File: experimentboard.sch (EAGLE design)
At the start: 173 parts, among them IC1 TL072P, IC2 LM317, IC3 LM337, IC4 TL072P, IC5 TL072P, IC6 TL072P, P1 PLR135/T9, P9 P9, U1 PCM1690, U2 DIR9001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

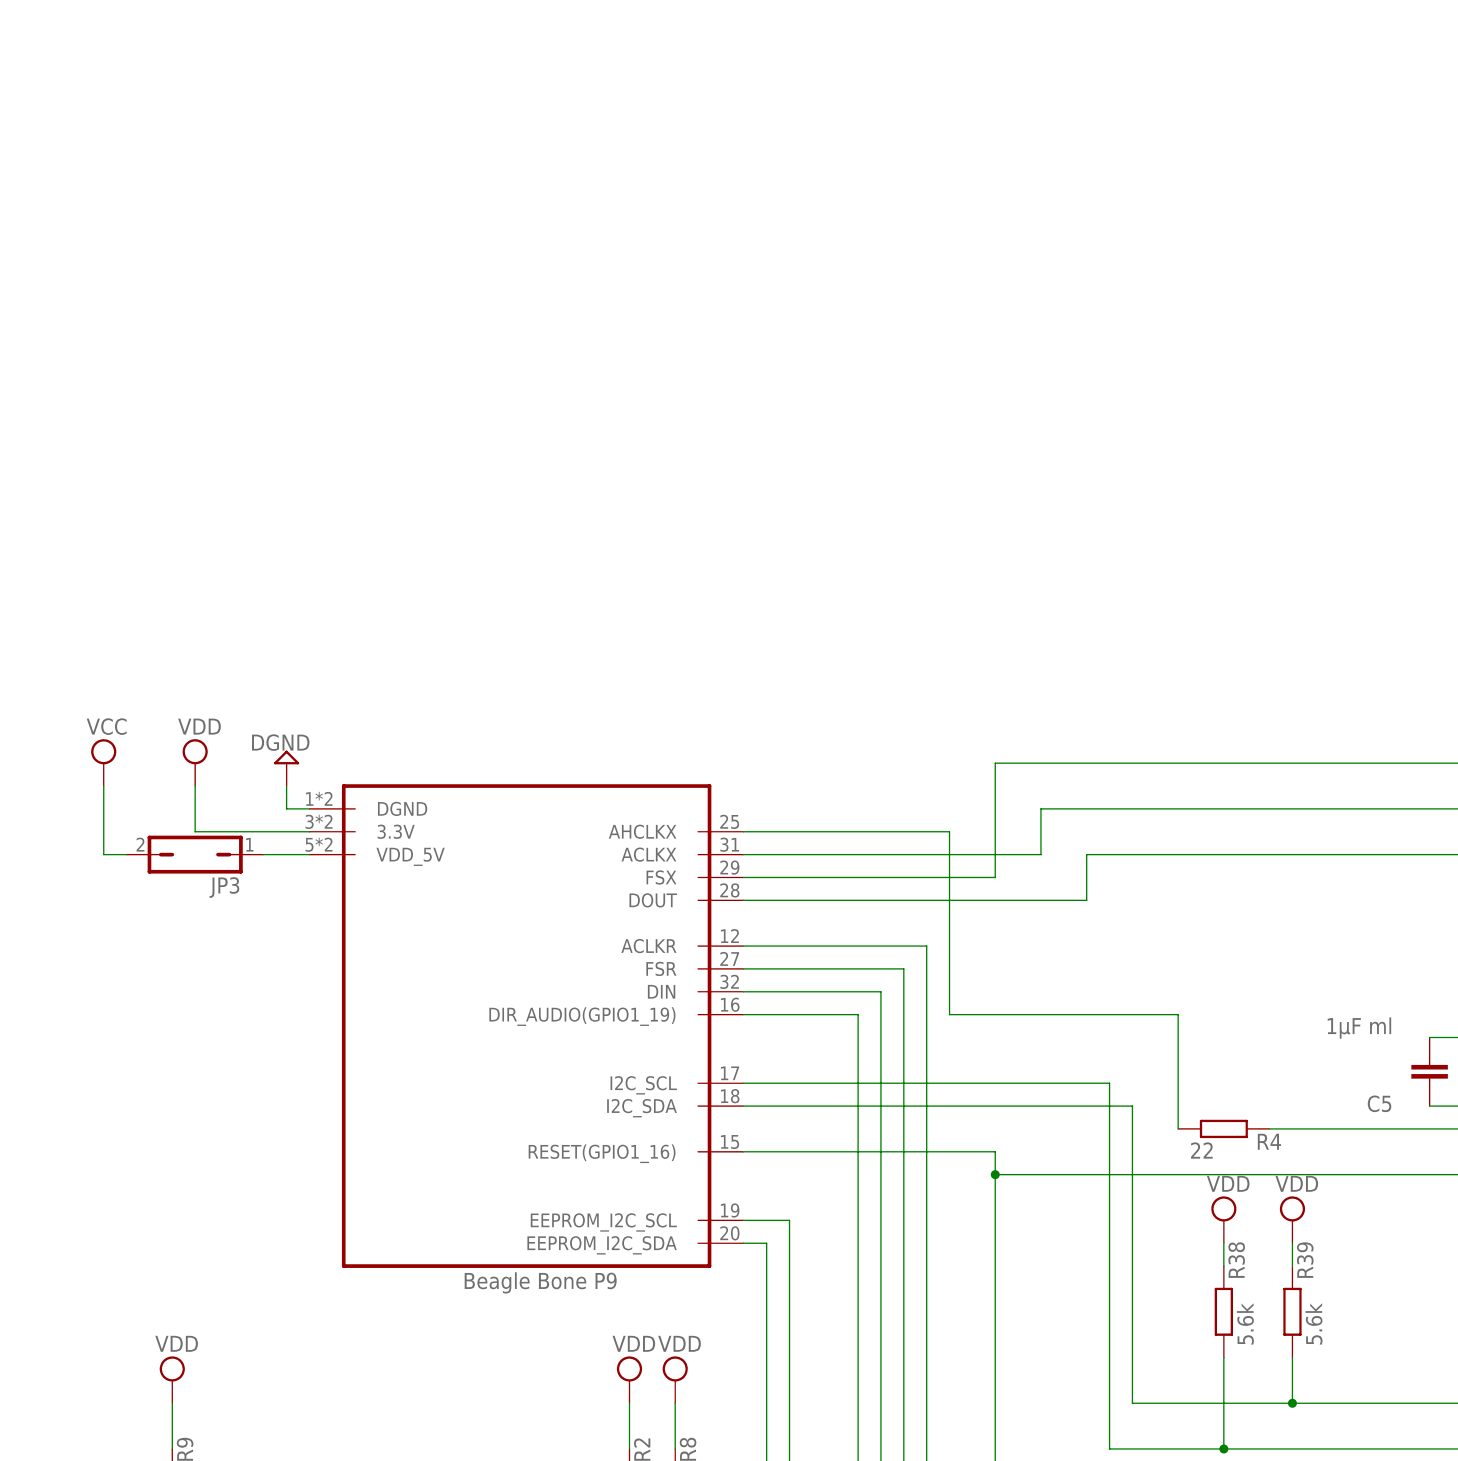
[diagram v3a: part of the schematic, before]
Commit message: Added two status LEDs
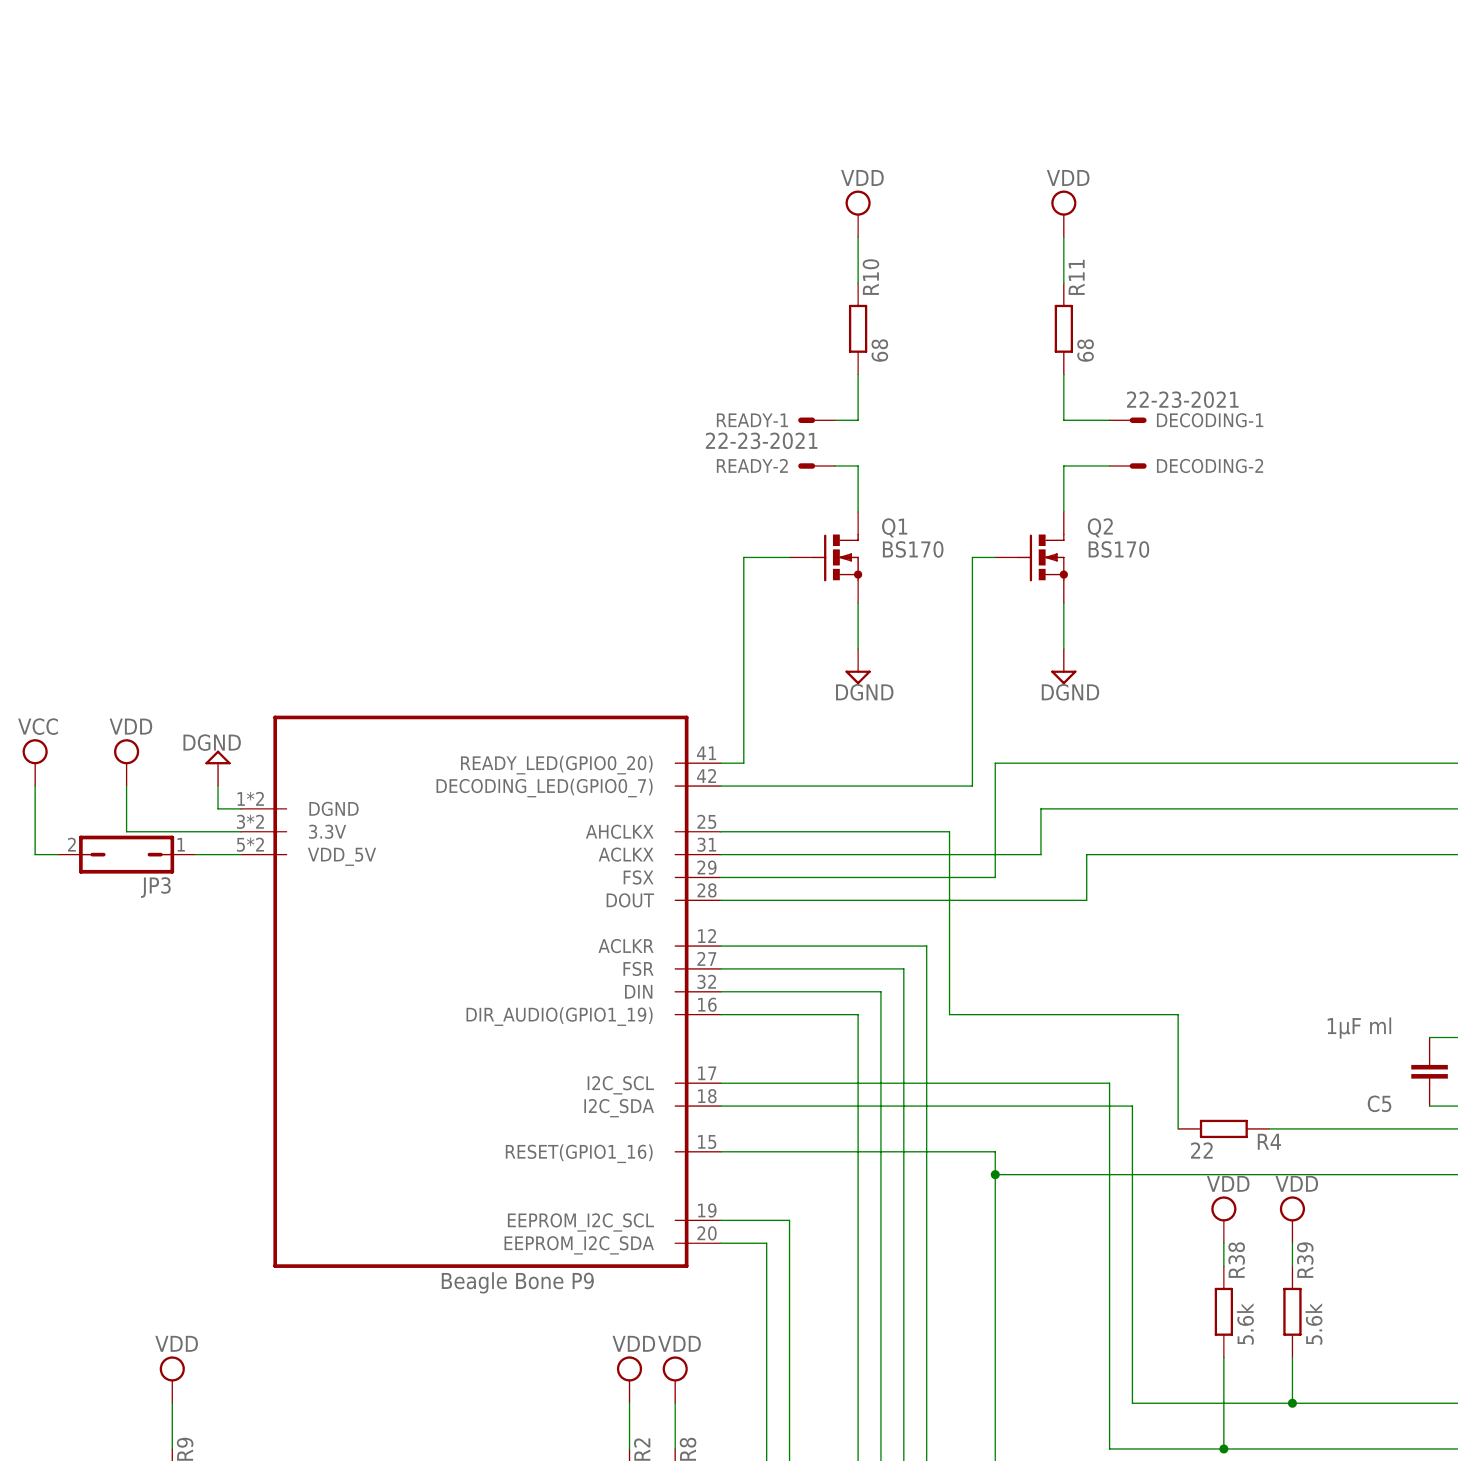
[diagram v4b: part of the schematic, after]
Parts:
- added DECODING, READY: 22-23-2021, con-molex:22-23-2021
- added Q1, Q2: BS170, transistor-small-signal:BS170
- added R10, R11: 68, rcl:R-EU_0204/2V
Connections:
- new net N$28: R10.1, READY-1.S
- new net N$4: Q1.D, READY-2.S
- new net N$91: DECODING-2.S, Q2.D
- new net N$92: DECODING-1.S, R11.1
- new net N$93: P9.READY_LED(GPIO0_20), Q1.G
- new net N$94: P9.DECODING_LED(GPIO0_7), Q2.G
- net DGND: now also Q1.S, Q2.S
- net VDD: now also R10.2, R11.2
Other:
- moved on the sheet: JP3

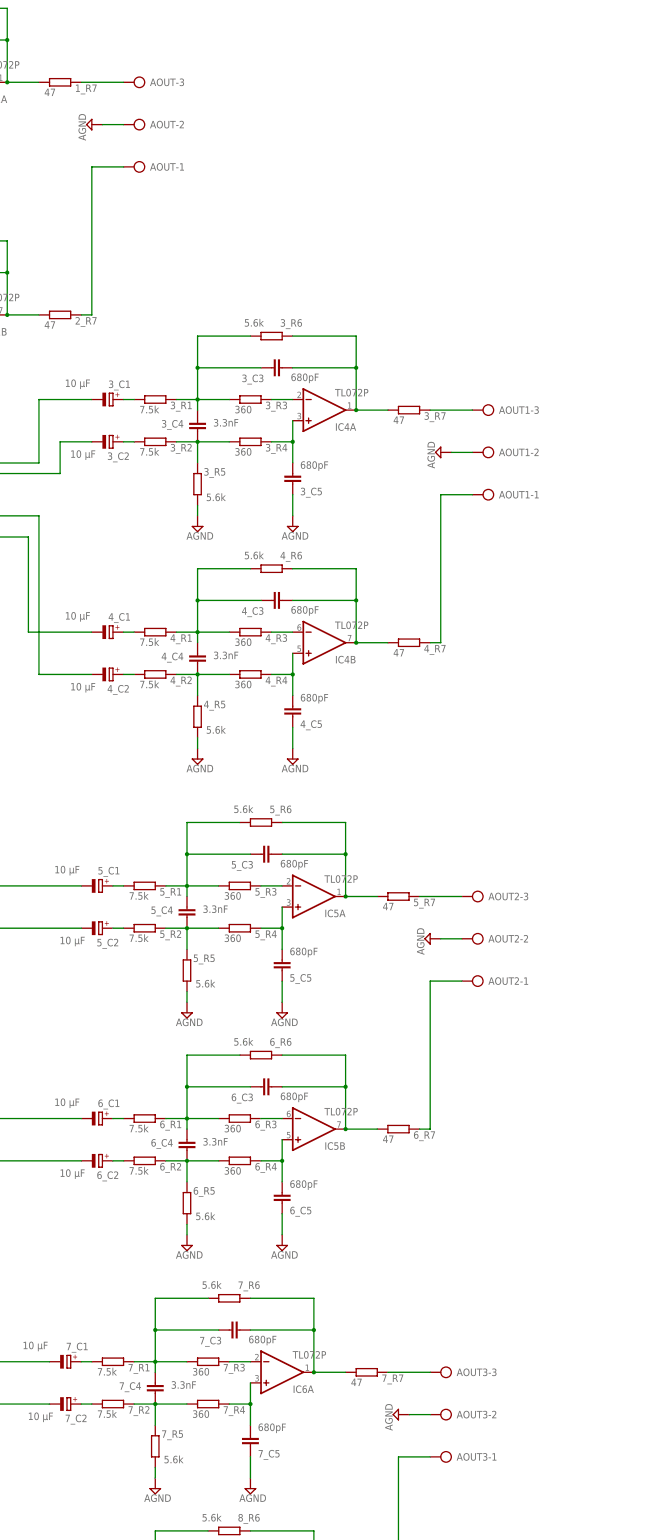
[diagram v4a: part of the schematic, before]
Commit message: Molex output connectors
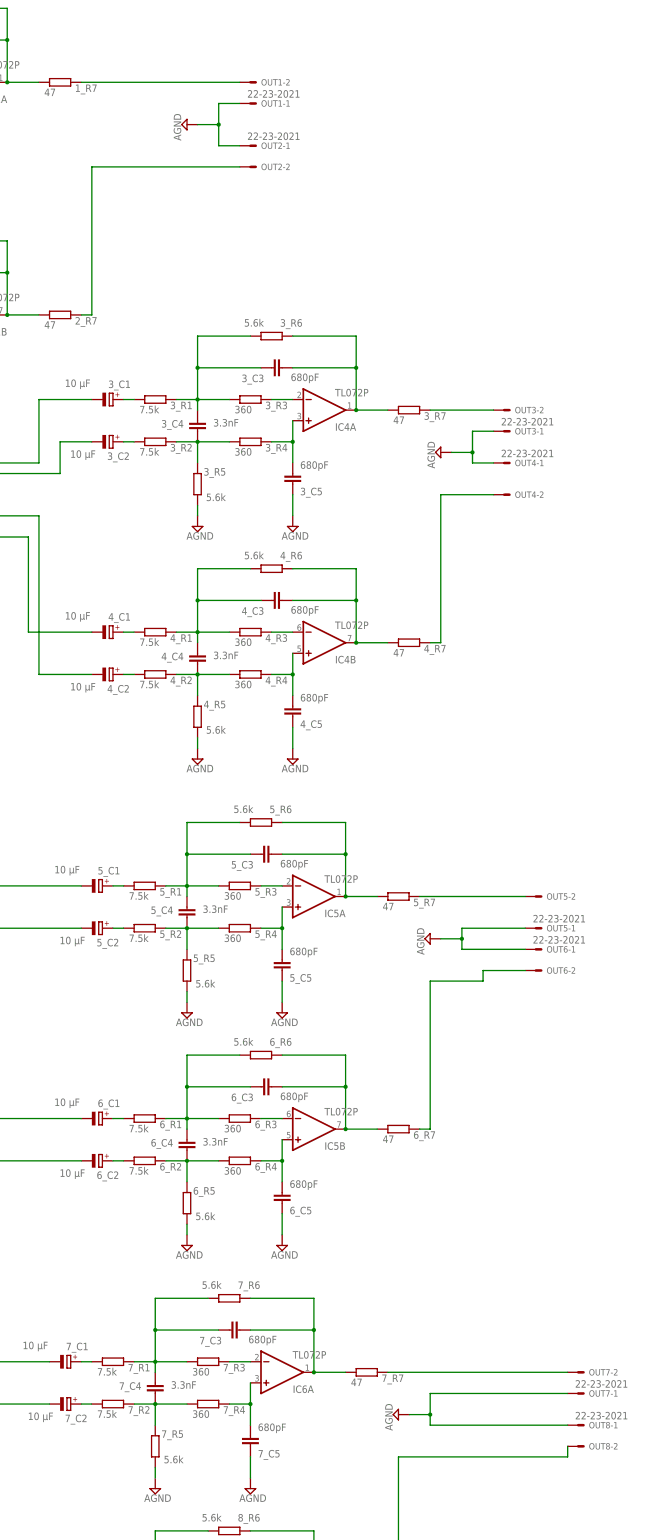
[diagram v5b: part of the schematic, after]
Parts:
- removed AOUT, AOUT1, AOUT2, AOUT3: (no value), con-ptr500:AK500/3
- added OUT1, OUT2, OUT3, OUT4, OUT5, OUT6, OUT7, OUT8: 22-23-2021, con-molex:22-23-2021
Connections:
- net AGND: now also OUT1-1.S, OUT2-1.S, OUT3-1.S, OUT4-1.S, OUT5-1.S, OUT6-1.S, OUT7-1.S, OUT8-1.S; no longer AOUT-2.KL, AOUT1-2.KL, AOUT2-2.KL, AOUT3-2.KL
- net N$37: now also OUT1-2.S; no longer AOUT-3.KL
- net N$38: now also OUT2-2.S; no longer AOUT-1.KL
- net N$64: now also OUT3-2.S; no longer AOUT1-3.KL
- net N$65: now also OUT4-2.S; no longer AOUT1-1.KL
- net N$82: now also OUT5-2.S; no longer AOUT2-3.KL
- net N$83: now also OUT6-2.S; no longer AOUT2-1.KL
- net N$89: now also OUT7-2.S; no longer AOUT3-3.KL
- net N$90: now also OUT8-2.S; no longer AOUT3-1.KL
